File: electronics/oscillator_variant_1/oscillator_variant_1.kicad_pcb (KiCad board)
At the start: 2 copper layers, 42.5 x 46.2 mm, 48 parts, among them J1 module_2x15_left_input, J2 module_2x15_right_input, J3 Coax, Q1 BC337, U1 TL081, U2 LME49720, U3 TL082, U4 TL431

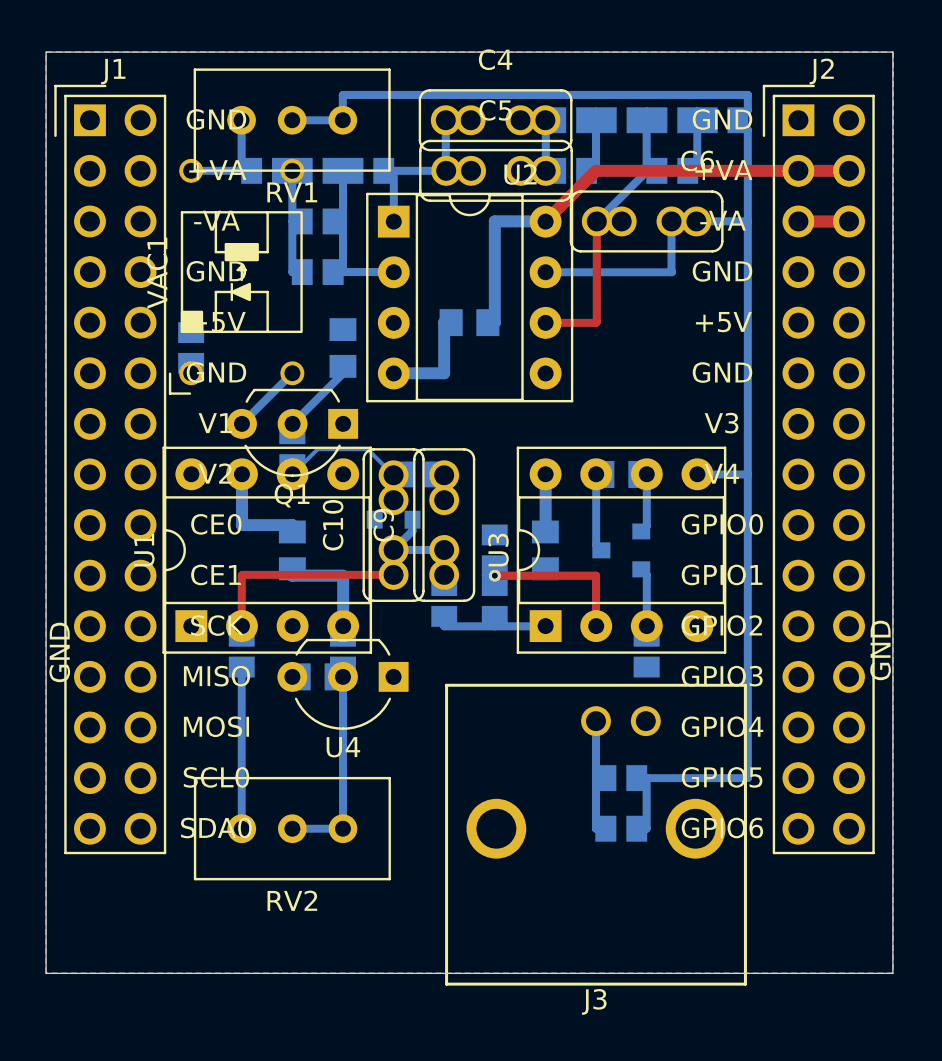
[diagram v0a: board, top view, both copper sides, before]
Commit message: placing and routing in progress, changed some ordering of resistors
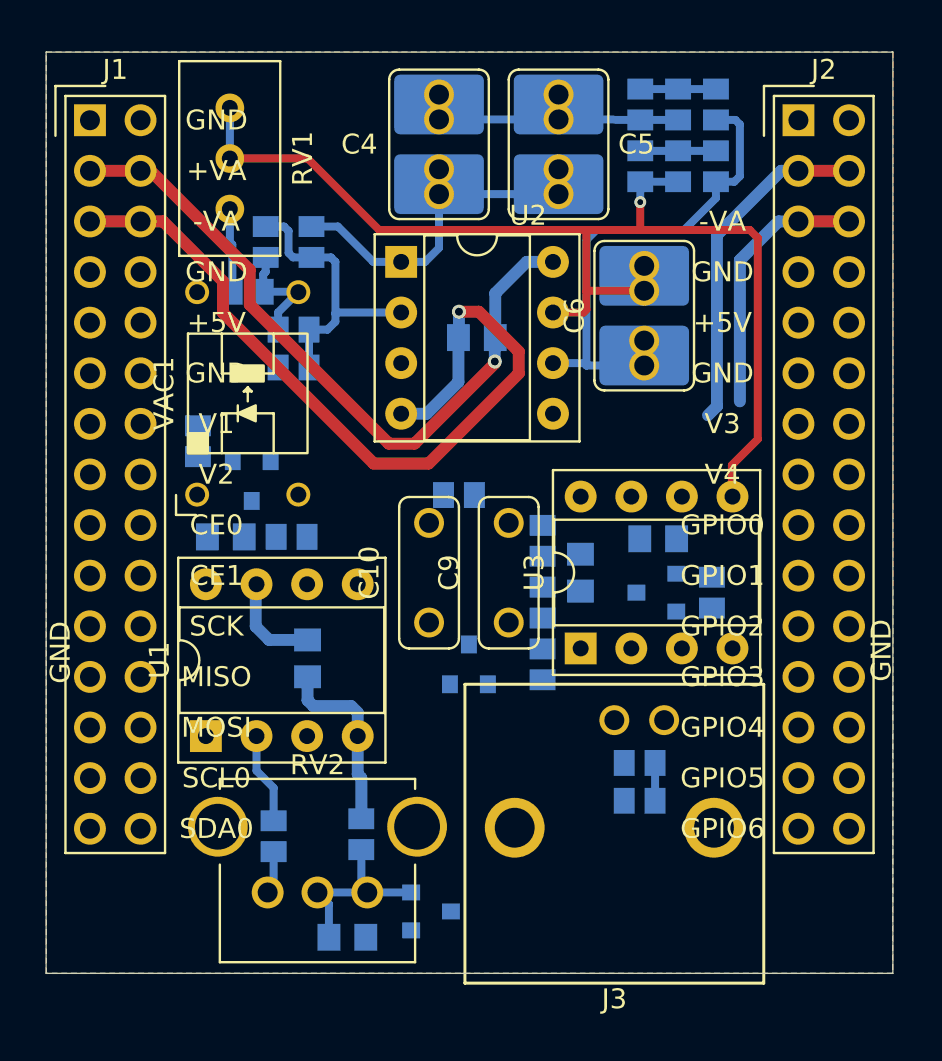
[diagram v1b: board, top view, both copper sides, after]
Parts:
- C10, C9: footprint SquantorRcl:C-025_050-030X100-film -> SquantorRcl:C-050-030X100-film
- C4, C5, C6: footprint SquantorRcl:C-025_050-030X100-film -> SquantorRcl:C-025_050-050X100-0805-3516-film
- Q1: value BC337 -> BC817; footprint Package_TO_SOT_THT:TO-92L_Inline_Wide -> SquantorIC:SOT23-3; moved to B.Cu
- RV2: footprint Potentiometer_THT:Potentiometer_Bourns_3296W_Vertical -> SquantorRcl:POT_ALPS_RK09K111
- U4: footprint Package_TO_SOT_THT:TO-92_Inline_Wide -> SquantorIC:SOT23-3; moved to B.Cu
- moved C8 13.2 mm to (157.7, 113.4), turned to 180 degrees
- moved U4 11.9 mm to (161.9, 112.1), turned to 0 degrees
- moved C11 11.2 mm to (151.6, 93.3), turned to 0 degrees
- moved N1 10.7 mm to (171.9, 114.2)
- moved N2 10.7 mm to (171.3, 110.3)
- moved R19 9.40 mm to (154.0, 108.3)
- moved R17 9.21 mm to (158.4, 108.2)
- moved D2 9.08 mm to (163.8, 99.7)
- moved R4 6.32 mm to (174.3, 71.6), turned to 90 degrees
- moved R9 6.15 mm to (152.7, 81.0)
- moved VAC1 6.10 mm to (152.7, 86.1)
- moved R18 5.88 mm to (167.5, 99.7), turned to 90 degrees
- moved U1 5.57 mm to (150.6, 103.3)
- moved R11 5.56 mm to (155.0, 82.9)
- moved C1 5.47 mm to (155.7, 99.4)
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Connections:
- C2 pad 1: -15V -> /-15_OSC
- C2 pad 2: +15V -> /+15_OSC
- J1 pad 3: +15V -> /+15_OSC
- J1 pad 4: +15V -> /+15_OSC
- J1 pad 5: -15V -> /-15_OSC
- J1 pad 6: -15V -> /-15_OSC
- R6 pad 1: Net-(C6-Pad1) -> Net-(R8-Pad1)
- R6 pad 2: Net-(R6-Pad2) -> /OUTPUT
- R7 pad 1: Net-(R6-Pad2) -> Net-(C6-Pad1)
- R7 pad 2: /OUTPUT -> Net-(R8-Pad1)
- R8 pad 1: Net-(C6-Pad1) -> Net-(R8-Pad1)
- R8 pad 2: Net-(R6-Pad2) -> /OUTPUT
- U2 pad 4: -15V -> /-15_OSC
- U2 pad 8: +15V -> /+15_OSC
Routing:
- net /-15_OSC: track 0.00 -> 41.3 mm, vias 0 -> 1
- net /+15_OSC: track 0.00 -> 35.8 mm, vias 0 -> 1
- net /OUTPUT: track 81.5 -> 59.1 mm, vias 0 -> 1
- net +15V: track 32.6 -> 22.2 mm
- net Net-(C10-Pad1): track 14.6 -> 4.61 mm
- net -15V: track 13.4 -> 22.7 mm
- net Net-(C4-Pad2): track 2.55 -> 11.9 mm
- net Net-(C6-Pad1): track 16.0 -> 24.3 mm
- net Net-(C4-Pad1): track 8.24 -> 16.1 mm
- net Net-(R14-Pad2): track 7.61 -> 0.00 mm, vias 1 -> 0
- net Net-(J3-Pad1): track 6.39 -> 0.00 mm
- net Net-(R10-Pad2): track 8.33 -> 14.6 mm
- net Net-(C10-Pad2): track 6.13 -> 0.00 mm
- net /GAIN_INPUT: track 6.08 -> 0.00 mm
- net Net-(R19-Pad2): track 8.12 -> 2.17 mm
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
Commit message: placing and routing further
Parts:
- R1, R13, R14, R15, R16, R17, R18, R19, R2, R20, R21: footprint SquantorRcl:R_0805+0603 -> SquantorRcl:R_0603_hand
- moved C11 7.30 mm to (156.4, 87.8), turned to 180 degrees
- moved R21 4.05 mm to (156.0, 89.4)
- moved R18 1.50 mm to (167.5, 98.2)
- moved R14 1.20 mm to (167.5, 95.4)
- moved C3 1.00 mm to (170.0, 94.3)
- moved R15 0.90 mm to (167.5, 92.6)
- moved R1 0.85 mm to (172.4, 105.7)
- moved R20 0.64 mm to (163.8, 90.8)
- moved R16 0.30 mm to (175.7, 96.1)
- moved R2 0.25 mm to (172.4, 104.4)
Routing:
- net -15V: track 22.7 -> 53.4 mm, vias 0 -> 2
- net +15V: track 22.2 -> 46.2 mm, vias 0 -> 2
- net Net-(C10-Pad2): track 0.00 -> 23.7 mm
- net /OUTPUT: track 59.1 -> 76.2 mm, vias 1 -> 2
- net Net-(C10-Pad1): track 4.61 -> 18.2 mm
- net Net-(C7-Pad2): track 0.00 -> 13.0 mm
- net Net-(R14-Pad2): track 0.00 -> 8.23 mm
- net Net-(C7-Pad1): track 0.00 -> 5.06 mm
- net Net-(C11-Pad2): track 0.00 -> 4.68 mm
- net /GAIN_INPUT: track 0.00 -> 4.41 mm
- net Net-(D1-Pad2): track 0.00 -> 3.50 mm
- net Net-(J3-Pad1): track 0.00 -> 3.39 mm
- net Net-(C9-Pad2): track 0.00 -> 2.66 mm
- net /GAIN: track 0.00 -> 2.47 mm
- net Net-(R9-Pad1): track 4.20 -> 5.98 mm
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
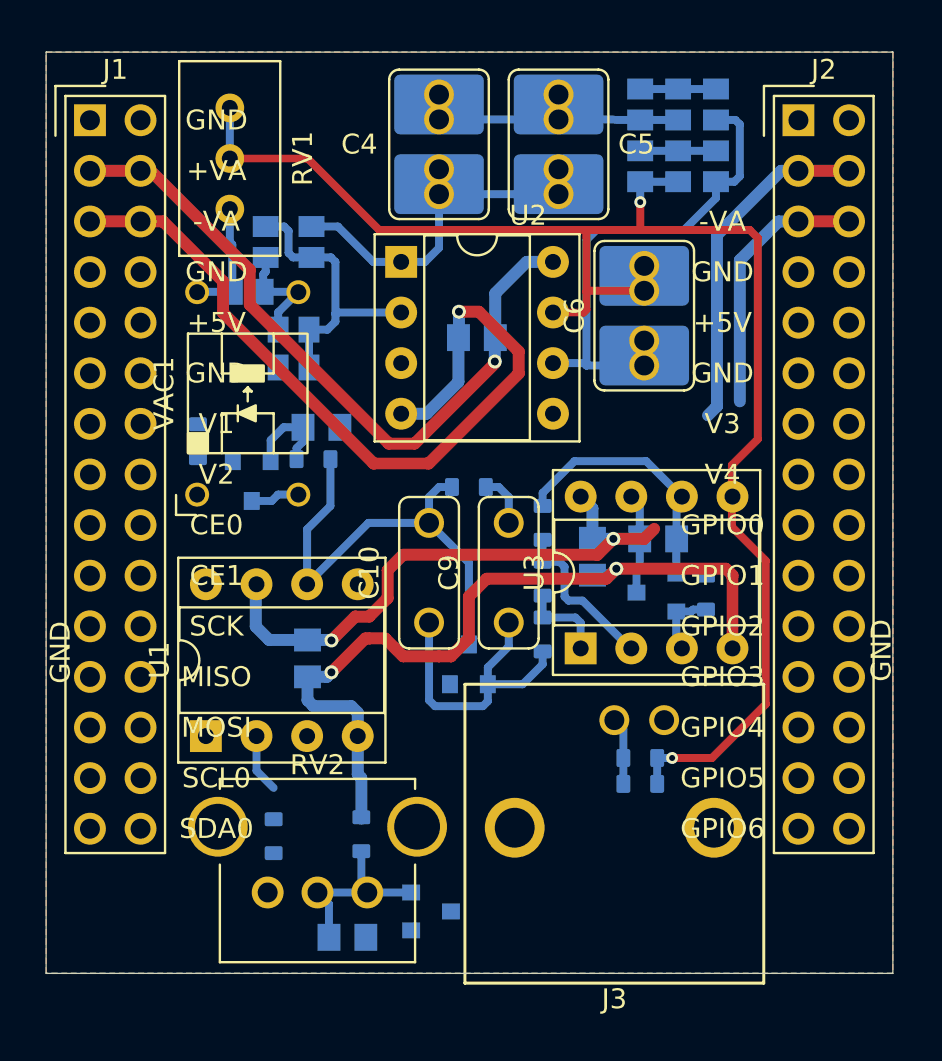
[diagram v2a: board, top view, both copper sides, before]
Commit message: updated some shielded components, changing routing of some nets keeping the ground plane as much contigious as possible
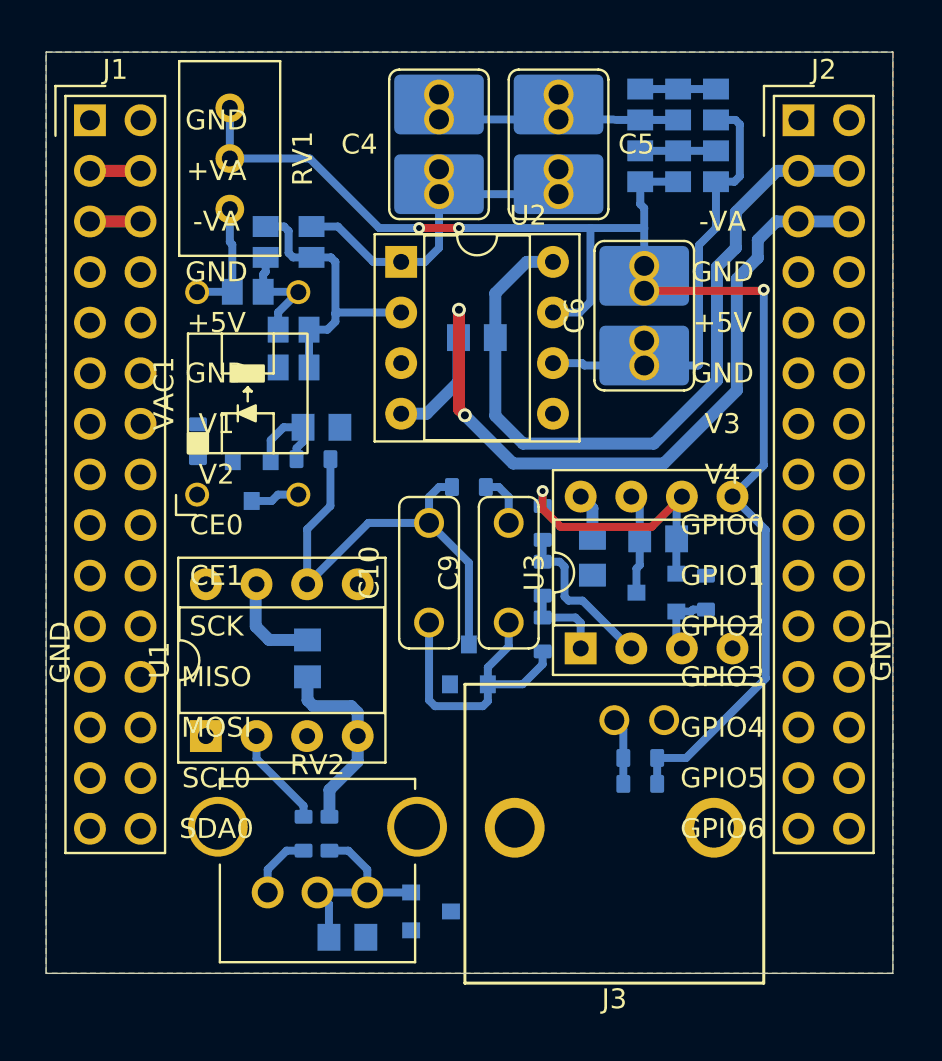
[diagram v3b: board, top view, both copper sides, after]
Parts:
- moved R17 1.60 mm to (156.8, 108.2)
- moved R19 1.51 mm to (155.5, 108.2)
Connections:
- J1 pad 3: /+15_OSC -> +15V
- J1 pad 4: /+15_OSC -> +15V
- J1 pad 5: /-15_OSC -> -15V
- J1 pad 6: /-15_OSC -> -15V
- J2 pad 3: +15V -> /+15_OSC
- J2 pad 4: +15V -> /+15_OSC
- J2 pad 5: -15V -> /-15_OSC
- J2 pad 6: -15V -> /-15_OSC
- RV2 pad S: (no net) -> GND
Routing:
- net -15V: track 53.4 -> 12.3 mm, vias 2 -> 0
- net +15V: track 46.2 -> 9.90 mm, vias 2 -> 0
- net /OUTPUT: track 76.2 -> 72.1 mm, vias 2 -> 3
- net Net-(R19-Pad2): track 0.42 -> 3.34 mm
- net /+15_OSC: track 35.8 -> 38.1 mm, vias 1 -> 0
- net Net-(C6-Pad1): track 24.3 -> 22.1 mm
- net Net-(C10-Pad1): track 18.2 -> 20.3 mm
- net Net-(C8-Pad2): track 9.46 -> 10.6 mm
- net Net-(C7-Pad2): track 13.0 -> 13.6 mm, vias 0 -> 1
- net /-15_OSC: track 41.3 -> 41.7 mm, vias 1 -> 2

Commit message: place and route and silk placement completed
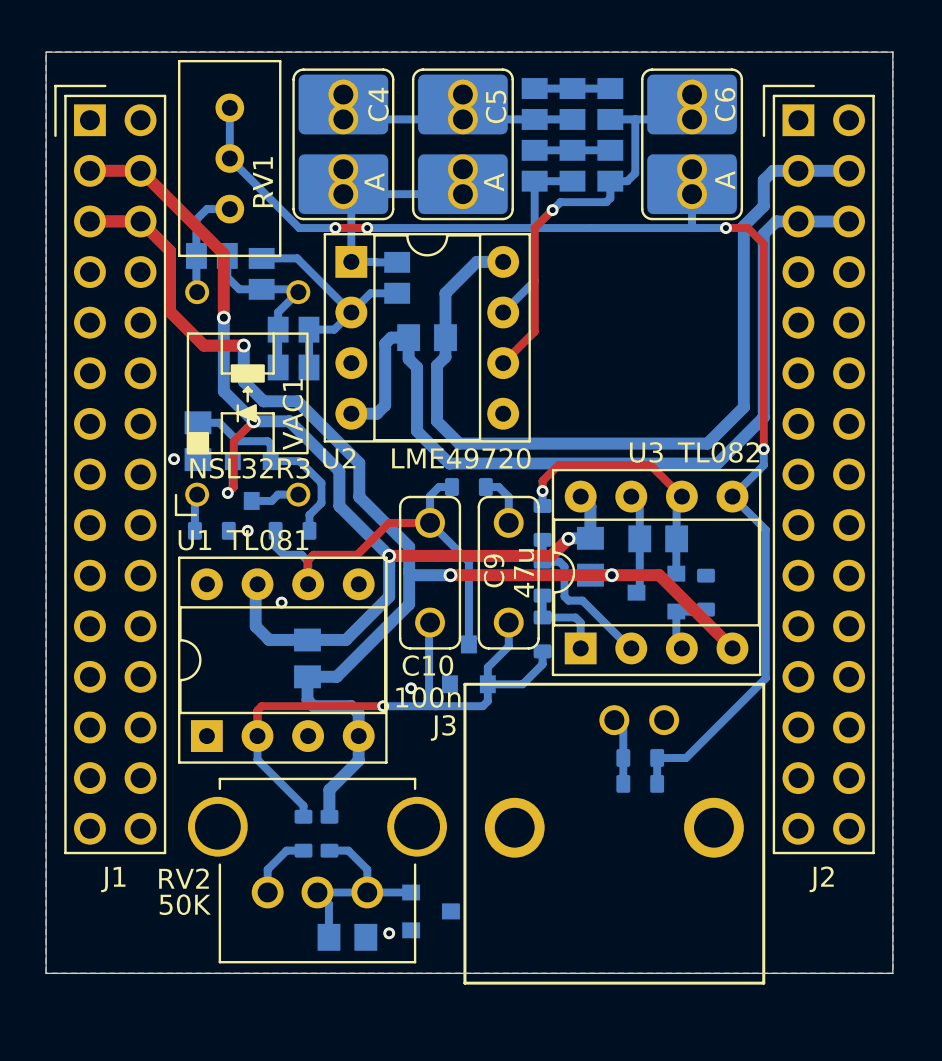
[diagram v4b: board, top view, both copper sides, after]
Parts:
- N1: value 20220428 -> 20220430
- R3: value B -> B/2
- R4: value C -> C/2
- R5: value D -> D/2
- moved C6 8.93 mm to (175.0, 73.6), turned to -90 degrees
- moved C11 6.24 mm to (150.2, 88.5), turned to 90 degrees
- moved R3 5.30 mm to (167.1, 71.6)
- moved R4 5.30 mm to (169.0, 71.6)
- moved R6 5.30 mm to (167.1, 74.7)
- moved R8 5.30 mm to (169.0, 74.7)
- moved R5 5.30 mm to (170.9, 71.6)
- moved R7 5.30 mm to (170.9, 74.7)
- moved C4 4.80 mm to (157.5, 73.6)
- moved C5 4.80 mm to (163.5, 73.6)
- moved R12 4.66 mm to (160.2, 80.3)
- moved R13 4.55 mm to (150.9, 93.0), turned to 180 degrees
- moved R21 3.75 mm to (154.9, 93.0), turned to 180 degrees
- moved R9 2.55 mm to (150.9, 79.2)
- moved C2 2.50 mm to (161.7, 83.3)
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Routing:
- net -15V: track 12.3 -> 64.9 mm, vias 0 -> 3
- net +15V: track 9.90 -> 58.8 mm, vias 0 -> 5
- net Net-(C10-Pad1): track 20.3 -> 30.6 mm, vias 0 -> 1
- net Net-(C11-Pad2): track 4.68 -> 10.6 mm
- net /+15_OSC: track 38.1 -> 43.1 mm
- net Net-(C4-Pad1): track 16.1 -> 11.9 mm
- net Net-(R10-Pad1): track 5.85 -> 9.15 mm
- net /-15_OSC: track 41.7 -> 43.9 mm, vias 2 -> 0
- net Net-(C10-Pad2): track 23.7 -> 21.6 mm
- net Net-(R10-Pad2): track 14.6 -> 12.7 mm
- net Net-(R13-Pad2): track 0.00 -> 1.87 mm
- net /OUTPUT: track 72.1 -> 73.5 mm, vias 3 -> 4
- net Net-(C6-Pad1): track 22.1 -> 20.9 mm, vias 0 -> 1
- net GND: vias 0 -> 5

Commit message: small modification made to select output point
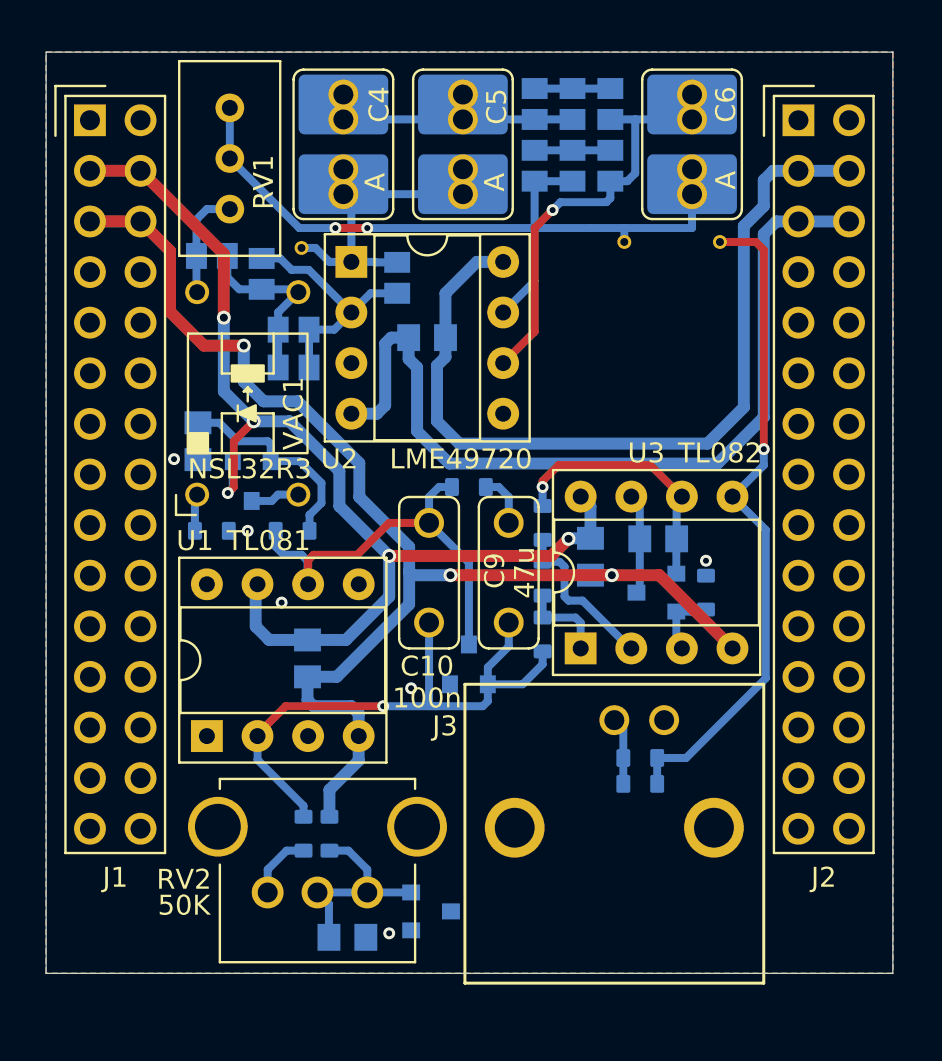
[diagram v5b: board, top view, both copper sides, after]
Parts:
- added TP1: out_gain, SquantorTestPoints:TestPoint_hole_H04R07, B.Cu at (155.4, 78.8)
- added TP2: out_wien, SquantorTestPoints:TestPoint_hole_H04R07, B.Cu at (171.6, 78.5)
- added TP3: output, SquantorTestPoints:TestPoint_hole_H04R07, B.Cu at (176.4, 78.5)
- N1: value 20220430 -> 20220501
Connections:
- net Net-(C4-Pad1) renamed /OUT_GAIN
- C6 pad 2: /OUTPUT -> /OUT_BRIDGE
- R6 pad 2: /OUTPUT -> /OUT_BRIDGE
- R8 pad 2: /OUTPUT -> /OUT_BRIDGE
- RV1 pad 2: /OUTPUT -> /OUT_BRIDGE
- RV1 pad 3: /OUTPUT -> /OUT_BRIDGE
- U2 pad 7: /OUTPUT -> /OUT_BRIDGE
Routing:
- net /OUTPUT: track 73.5 -> 33.6 mm, vias 4 -> 1
- net /OUT_BRIDGE: track 0.00 -> 38.7 mm, vias 0 -> 2
- net /OUT_GAIN: track 11.9 -> 14.7 mm
- net Net-(C10-Pad1): track 30.6 -> 29.8 mm
- net GND: vias 5 -> 6
